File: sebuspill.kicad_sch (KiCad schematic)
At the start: 26 parts, among them J1 Conn_01x04_Male, J2 USB_B_Micro, J3 Pinout 1, J4 Pinout 2, SW1 SW_SPDT, U1 AMS1117-3.3, U2 STM32F103C8T6, Y1 16MHz

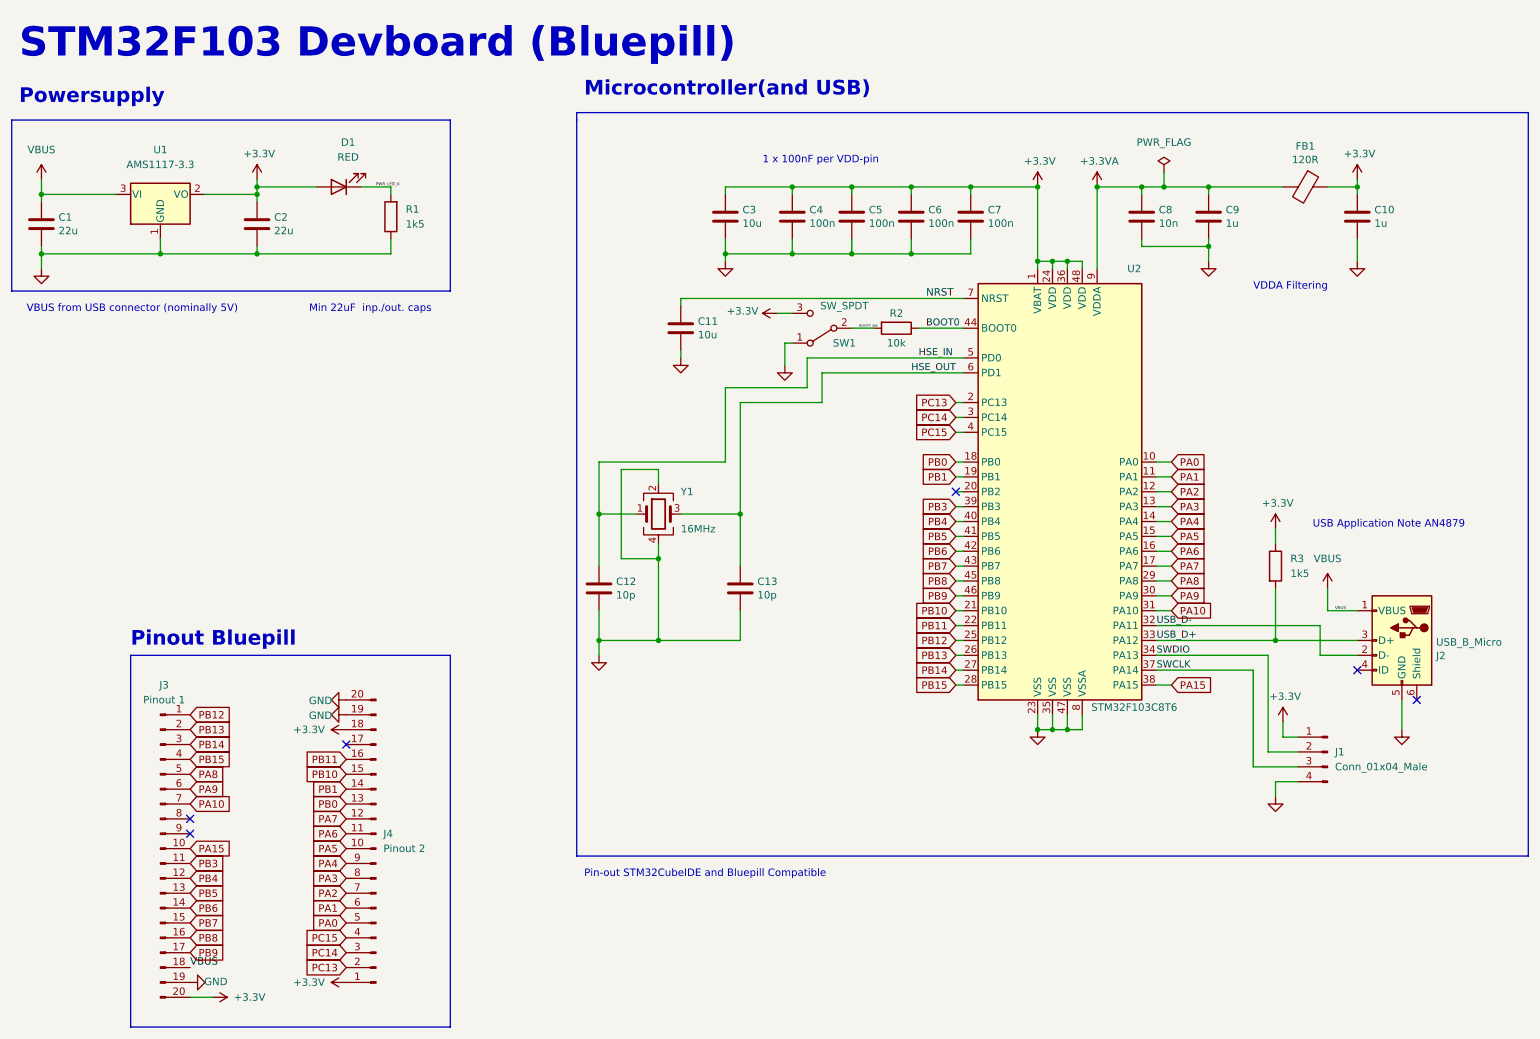
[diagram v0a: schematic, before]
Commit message: added all components, next step routing and outline
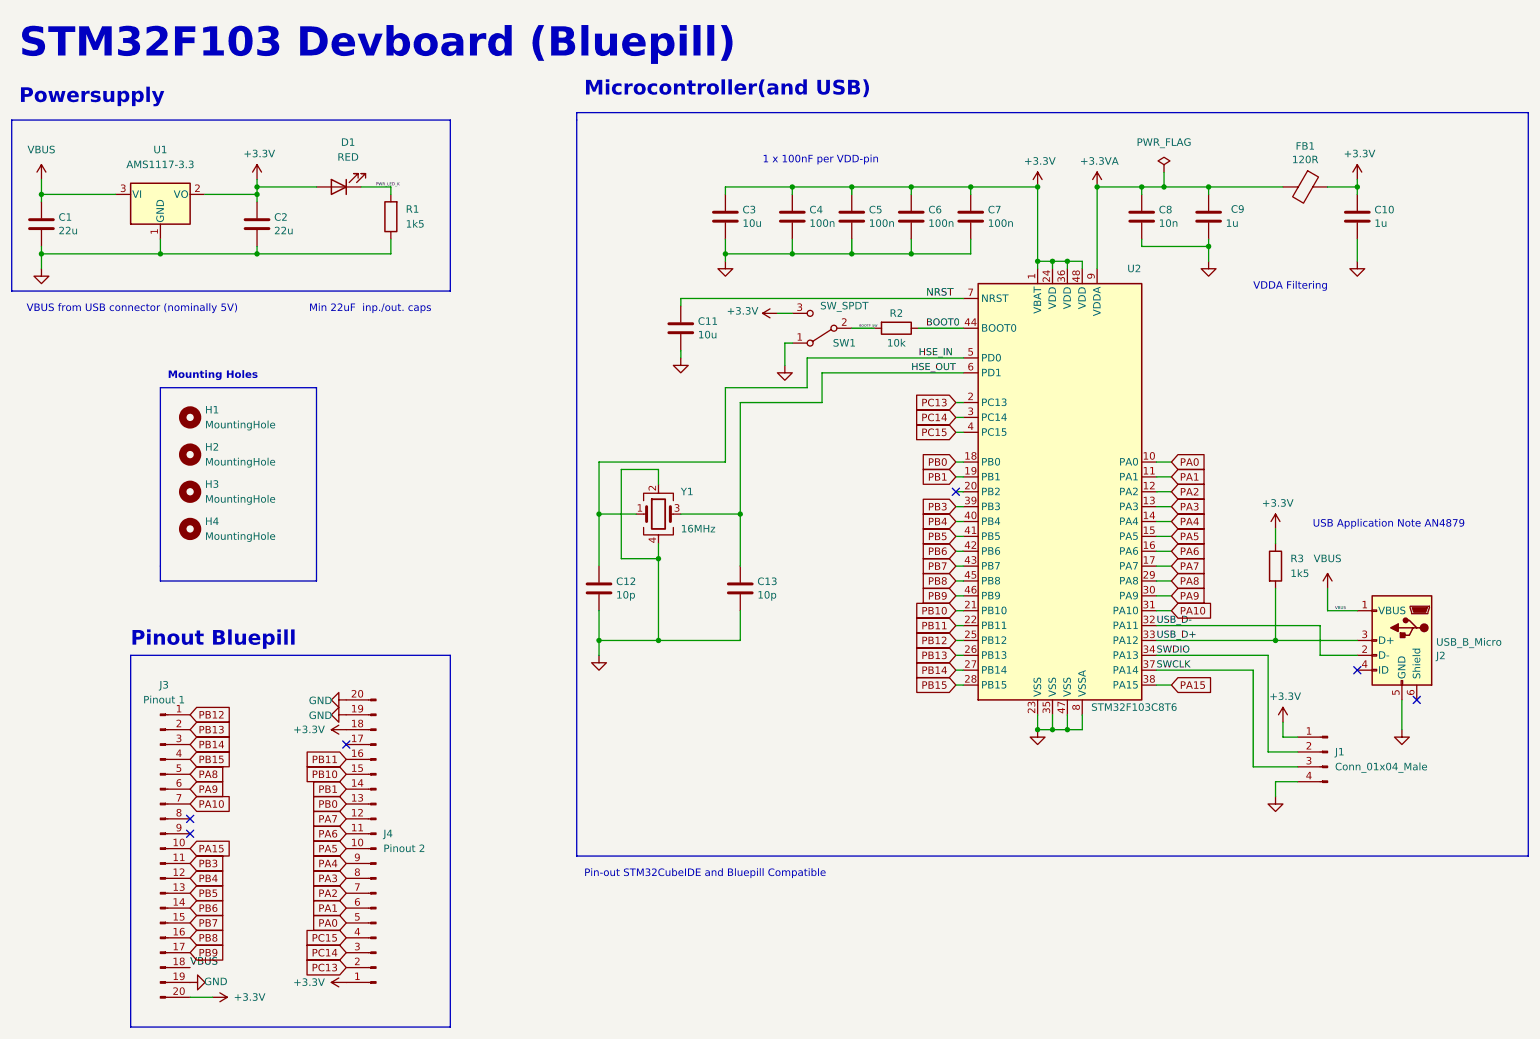
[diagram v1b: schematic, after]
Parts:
- added H1, H2, H3, H4: MountingHole, MountingHole:MountingHole_2.2mm_M2, symbol Mechanical:MountingHole
- SW1: footprint Button_Switch_THT:SW_Lever_1P2T_NKK_GW12LxH -> Button_Switch_SMD:SW_SPDT_PCM12
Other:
- note added: "Mounting Holes"
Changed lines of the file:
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@@
+    (stroke (width 0) (type default) (color 0 0 0 0))
+  )
+  (polyline (pts (xy 43.18 109.22) (xy 43.18 78.74))
     (stroke (width 0) (type default) (color 0 0 0 0))
   )
@@
     (stroke (width 0) (type default) (color 0 0 0 0))
   )
+  (polyline (pts (xy 69.85 78.74) (xy 69.85 111.76))
+    (stroke (width 0) (type default) (color 0 0 0 0))
+  )
   (wire (pts (xy 118.11 100.33) (xy 118.11 109.22))
     (stroke (width 0) (type default) (color 0 0 0 0))
@@
     (stroke (width 0) (type default) (color 0 0 0 0))
   )
+  (polyline (pts (xy 69.85 111.76) (xy 43.18 111.76))
+    (stroke (width 0) (type default) (color 0 0 0 0))
+  )
   (wire (pts (xy 128.27 92.71) (xy 128.27 95.25))
     (stroke (width 0) (type default) (color 0 0 0 0))
@@
     (stroke (width 0) (type default) (color 0 0 0 0))
   )
+  (polyline (pts (xy 43.18 78.74) (xy 69.85 78.74))
+    (stroke (width 0) (type default) (color 0 0 0 0))
+  )
   (wire (pts (xy 210.82 53.34) (xy 210.82 54.61))
     (stroke (width 0) (type default) (color 0 0 0 0))
@@
   )
   (wire (pts (xy 118.11 100.33) (xy 118.11 91.44))
+    (stroke (width 0) (type default) (color 0 0 0 0))
+  )
+  (polyline (pts (xy 43.18 109.22) (xy 43.18 111.76))
     (stroke (width 0) (type default) (color 0 0 0 0))
   )
@@
   (text "Pinout Bluepill" (at 38.1 123.19 0)
     (effects (font (size 2.5 2.5) (thickness 0.5) bold) (justify left bottom))
+  )
+  (text "Mounting Holes" (at 44.45 77.47 0)
+    (effects (font (size 1.27 1.27) (thickness 0.254) bold) (justify left bottom))
   )
   (text "USB Application Note AN4879" (at 240.03 102.87 0)
@@
   (symbol (lib_id "Device:C") (at 222.25 49.53 0) (unit 1)
     (in_bom yes) (on_board yes)
-    (property "Reference" "C9" (id 0) (at 225.171 48.3616 0)
+    (property "Reference" "C9" (id 0) (at 226.06 48.26 0)
       (effects (font (size 1.27 1.27)) (justify left))
     )
@@
     (property "Reference" "SW1" (id 0) (at 160.02 71.12 0))
     (property "Value" "SW_SPDT" (id 1) (at 160.02 64.77 0))
-    (property "Footprint" "Button_Switch_THT:SW_Lever_1P2T_NKK_GW12LxH" (id 2) (at 156.21 68.58 0)
+    (property "Footprint" "Button_Switch_SMD:SW_SPDT_PCM12" (id 2) (at 156.21 68.58 0)
       (effects (font (size 1.27 1.27)) hide)
     )
@@
     )
     (pin "1")
+  )
+  (symbol (lib_id "Mechanical:MountingHole") (at 48.26 83.82 0) (unit 1)
+    (in_bom yes) (on_board yes) (fields_autoplaced)
+    (property "Reference" "H1" (id 0) (at 50.8 82.5499 0)
+      (effects (font (size 1.27 1.27)) (justify left))
+    )
+    (property "Value" "MountingHole" (id 1) (at 50.8 85.0899 0)
+      (effects (font (size 1.27 1.27)) (justify left))
+    )
+    (property "Footprint" "MountingHole:MountingHole_2.2mm_M2" (id 2) (at 48.26 83.82 0)
+      (effects (font (size 1.27 1.27)) hide)
+    )
+    (property "Datasheet" "~" (id 3) (at 48.26 83.82 0)
+      (effects (font (size 1.27 1.27)) hide)
+    )
   )
   (symbol (lib_id "Device:LED") (at 73.66 44.45 180) (unit 1)
@@
     (pin "1")
   )
+  (symbol (lib_id "Mechanical:MountingHole") (at 48.26 96.52 0) (unit 1)
+    (in_bom yes) (on_board yes) (fields_autoplaced)
+    (property "Reference" "H3" (id 0) (at 50.8 95.2499 0)
+      (effects (font (size 1.27 1.27)) (justify left))
+    )
+    (property "Value" "MountingHole" (id 1) (at 50.8 97.7899 0)
+      (effects (font (size 1.27 1.27)) (justify left))
+    )
+    (property "Footprint" "MountingHole:MountingHole_2.2mm_M2" (id 2) (at 48.26 96.52 0)
+      (effects (font (size 1.27 1.27)) hide)
+    )
+    (property "Datasheet" "~" (id 3) (at 48.26 96.52 0)
+      (effects (font (size 1.27 1.27)) hide)
+    )
+  )
   (symbol (lib_id "power:GND") (at 74.93 132.08 270) (unit 1)
     (in_bom yes) (on_board yes)
@@
     )
     (pin "1")
+  )
+  (symbol (lib_id "Mechanical:MountingHole") (at 48.26 102.87 0) (unit 1)
+    (in_bom yes) (on_board yes) (fields_autoplaced)
+    (property "Reference" "H4" (id 0) (at 50.8 101.5999 0)
+      (effects (font (size 1.27 1.27)) (justify left))
+    )
+    (property "Value" "MountingHole" (id 1) (at 50.8 104.1399 0)
+      (effects (font (size 1.27 1.27)) (justify left))
+    )
+    (property "Footprint" "MountingHole:MountingHole_2.2mm_M2" (id 2) (at 48.26 102.87 0)
+      (effects (font (size 1.27 1.27)) hide)
+    )
+    (property "Datasheet" "~" (id 3) (at 48.26 102.87 0)
+      (effects (font (size 1.27 1.27)) hide)
+    )
   )
   (symbol (lib_id "Connector:Conn_01x20_Male") (at 80.01 157.48 180) (unit 1)
@@
     (pin "9")
   )
+  (symbol (lib_id "Mechanical:MountingHole") (at 48.26 90.17 0) (unit 1)
+    (in_bom yes) (on_board yes) (fields_autoplaced)
+    (property "Reference" "H2" (id 0) (at 50.8 88.8999 0)
+      (effects (font (size 1.27 1.27)) (justify left))
+    )
+    (property "Value" "MountingHole" (id 1) (at 50.8 91.4399 0)
+      (effects (font (size 1.27 1.27)) (justify left))
+    )
+    (property "Footprint" "MountingHole:MountingHole_2.2mm_M2" (id 2) (at 48.26 90.17 0)
+      (effects (font (size 1.27 1.27)) hide)
+    )
+    (property "Datasheet" "~" (id 3) (at 48.26 90.17 0)
+      (effects (font (size 1.27 1.27)) hide)
+    )
+  )
   (symbol (lib_id "Connector:Conn_01x04_Male") (at 242.57 140.97 0) (mirror y) (unit 1)
     (in_bom yes) (on_board yes) (fields_autoplaced)
@@
       (reference "FB1") (unit 1) (value "120R") (footprint "Inductor_SMD:L_0603_1608Metric")
     )
+    (path "/3e17c8d9-7272-45e7-8563-368bbe0cc392"
+      (reference "H1") (unit 1) (value "MountingHole") (footprint "MountingHole:MountingHole_2.2mm_M2")
+    )
+    (path "/962db9f5-a982-4c6b-a3b5-c0157fc784a7"
+      (reference "H2") (unit 1) (value "MountingHole") (footprint "MountingHole:MountingHole_2.2mm_M2")
+    )
+    (path "/69877790-6384-4f64-822e-136b0b731636"
+      (reference "H3") (unit 1) (value "MountingHole") (footprint "MountingHole:MountingHole_2.2mm_M2")
+    )
+    (path "/8616b25d-fde3-495b-a95b-01af35f50dec"
+      (reference "H4") (unit 1) (value "MountingHole") (footprint "MountingHole:MountingHole_2.2mm_M2")
+    )
     (path "/a41b66fb-229f-4bdc-9b73-542cf6482879"
       (reference "J1") (unit 1) (value "Conn_01x04_Male") (footprint "Connector_PinHeader_2.54mm:PinHeader_1x04_P2.54mm_Vertical")
@@
     )
     (path "/00000000-0000-0000-0000-000066eb70a8"
-      (reference "SW1") (unit 1) (value "SW_SPDT") (footprint "Button_Switch_THT:SW_Lever_1P2T_NKK_GW12LxH")
+      (reference "SW1") (unit 1) (value "SW_SPDT") (footprint "Button_Switch_SMD:SW_SPDT_PCM12")
     )
     (path "/54ffd941-bf6e-4fd9-a4f5-b0eda470cff6"

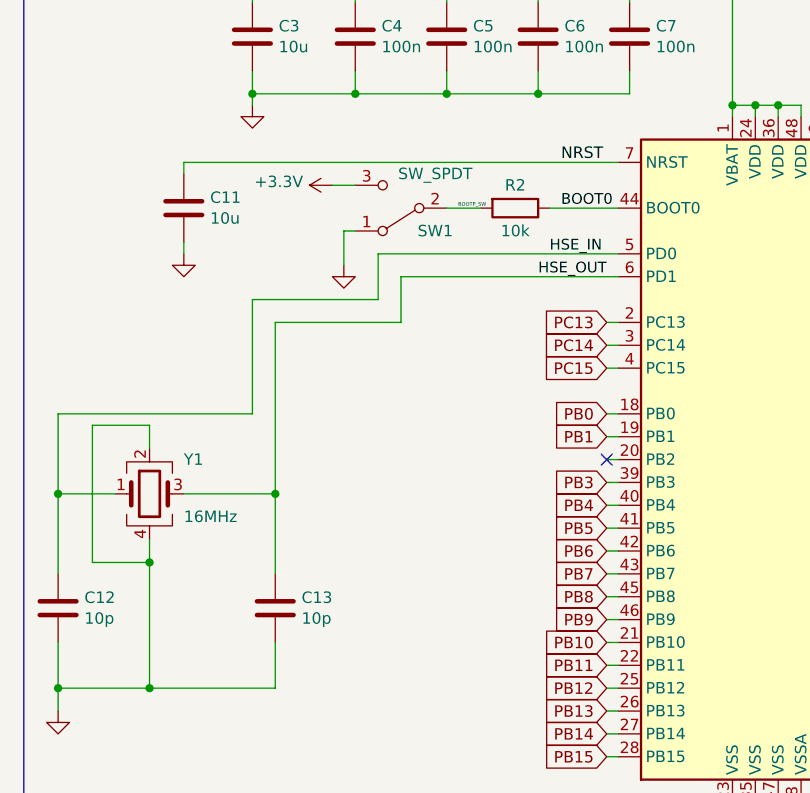
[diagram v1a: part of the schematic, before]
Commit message: changed SMD switch to Jumper bc JLCPCB hat no in stock and added User programmable LED to PC13
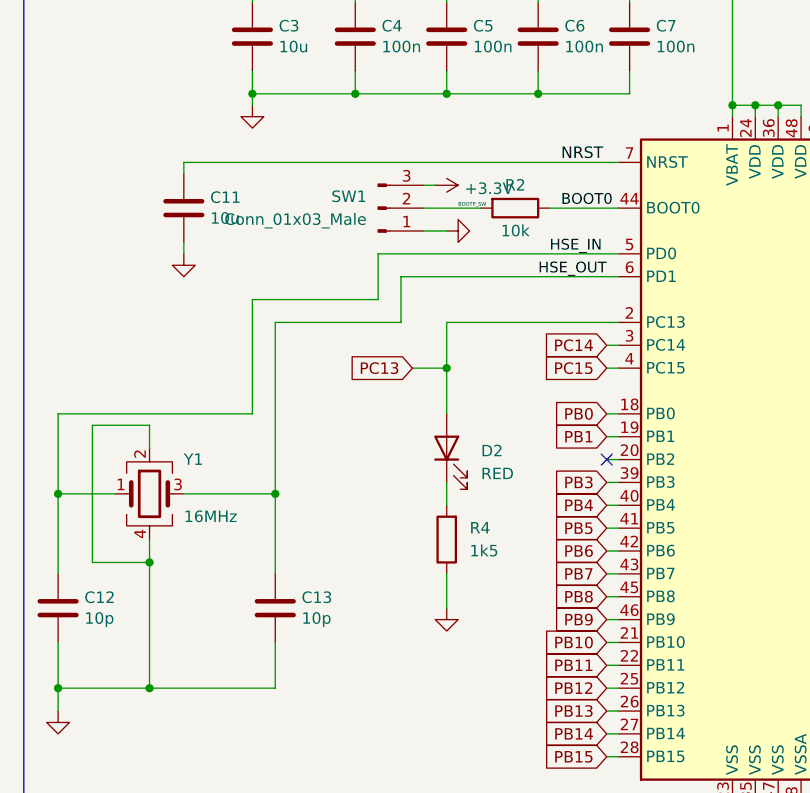
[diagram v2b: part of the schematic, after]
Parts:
- removed SW1: SW_SPDT, Button_Switch_SMD:SW_SPDT_PCM12, symbol Switch:SW_SPDT
- added D2: RED, LED_SMD:LED_0603_1608Metric, symbol Device:LED
- added R4: 1k5, Resistor_SMD:R_0402_1005Metric, symbol Device:R
- added SW1: Conn_01x03_Male, symbol Connector:Conn_01x03_Male
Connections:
- net +3V3: now also SW1.3 (Pin_3)
- net BOOTP_SW: now also SW1.2 (Pin_2)
- net GND: now also R4.1, SW1.1 (Pin_1)
- net PC13: now also D2.2 (A)
- new net: D2.1 (K), R4.2
